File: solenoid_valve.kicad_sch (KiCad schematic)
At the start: 7 parts, among them J17 Conn_01x02_Socket, Q1 Q_NMOS_GSD, U9 TLP785

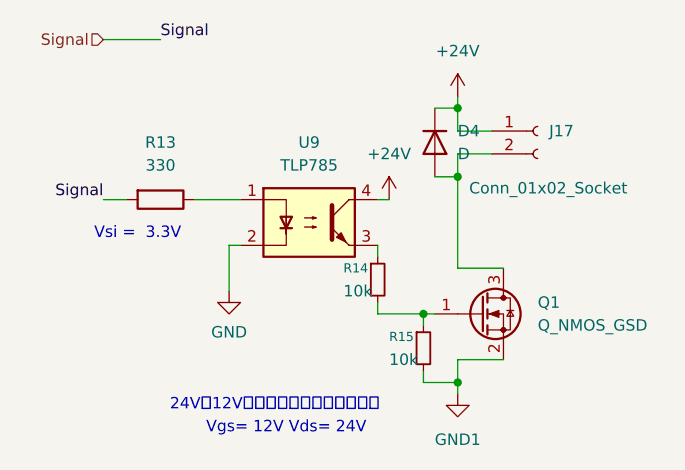
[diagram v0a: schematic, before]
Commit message: サーボときんていをつけ忘れていたので回路図に追加(部品配置に悩んでる
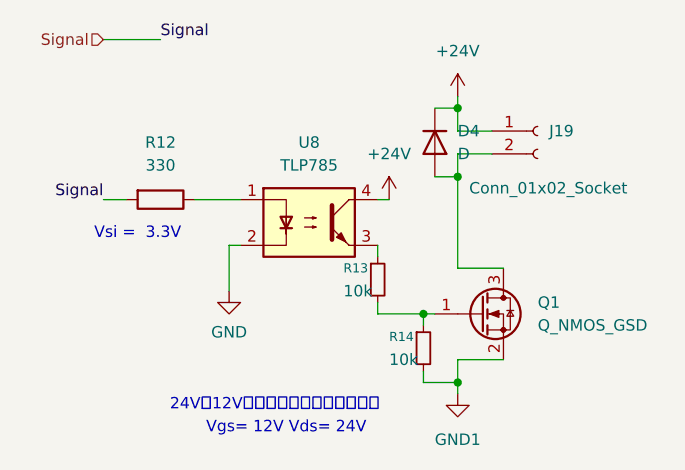
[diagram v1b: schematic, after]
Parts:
- renumbered J17 to J19, R13 to R12, R14 to R13, R15 to R14, U9 to U8
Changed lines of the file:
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@@
 		(in_pos_files yes)
 		(dnp no)
-		(property "Reference" "J17"
+		(property "Reference" "J19"
 			(at 130.81 59.6899 0)
 			(show_name no)
@@
 			(project "ARSTM2602"
 				(path "/537f457d-9719-41ea-89c7-39afb0f25936/1b1d3c2c-89c2-4210-b4e2-6e7b33b504ab"
+					(reference "J22")
+					(unit 1)
+				)
+				(path "/537f457d-9719-41ea-89c7-39afb0f25936/3c4eddd9-2f6c-48df-bbb7-01288ca35755"
+					(reference "J21")
+					(unit 1)
+				)
+				(path "/537f457d-9719-41ea-89c7-39afb0f25936/70727c92-d750-4c7e-95c8-20e0820def0e"
+					(reference "J19")
+					(unit 1)
+				)
+				(path "/537f457d-9719-41ea-89c7-39afb0f25936/884f7e7d-b238-4bb6-a1d8-53bdfde88689"
+					(reference "J23")
+					(unit 1)
+				)
+				(path "/537f457d-9719-41ea-89c7-39afb0f25936/e0dbbca2-494e-4b2c-9270-2b014d7f4a27"
 					(reference "J20")
-					(unit 1)
-				)
-				(path "/537f457d-9719-41ea-89c7-39afb0f25936/3c4eddd9-2f6c-48df-bbb7-01288ca35755"
-					(reference "J19")
-					(unit 1)
-				)
-				(path "/537f457d-9719-41ea-89c7-39afb0f25936/70727c92-d750-4c7e-95c8-20e0820def0e"
-					(reference "J17")
-					(unit 1)
-				)
-				(path "/537f457d-9719-41ea-89c7-39afb0f25936/884f7e7d-b238-4bb6-a1d8-53bdfde88689"
-					(reference "J21")
-					(unit 1)
-				)
-				(path "/537f457d-9719-41ea-89c7-39afb0f25936/e0dbbca2-494e-4b2c-9270-2b014d7f4a27"
-					(reference "J18")
 					(unit 1)
 				)
@@
 		(dnp no)
 		(fields_autoplaced yes)
-		(property "Reference" "#PWR052"
+		(property "Reference" "#PWR057"
 			(at 120.65 59.69 0)
 			(hide yes)
@@
 			(project "ARSTM2602"
 				(path "/537f457d-9719-41ea-89c7-39afb0f25936/1b1d3c2c-89c2-4210-b4e2-6e7b33b504ab"
-					(reference "#PWR064")
+					(reference "#PWR069")
 					(unit 1)
 				)
 				(path "/537f457d-9719-41ea-89c7-39afb0f25936/3c4eddd9-2f6c-48df-bbb7-01288ca35755"
-					(reference "#PWR060")
+					(reference "#PWR065")
 					(unit 1)
 				)
 				(path "/537f457d-9719-41ea-89c7-39afb0f25936/70727c92-d750-4c7e-95c8-20e0820def0e"
-					(reference "#PWR052")
+					(reference "#PWR057")
 					(unit 1)
 				)
 				(path "/537f457d-9719-41ea-89c7-39afb0f25936/884f7e7d-b238-4bb6-a1d8-53bdfde88689"
-					(reference "#PWR068")
+					(reference "#PWR073")
 					(unit 1)
 				)
 				(path "/537f457d-9719-41ea-89c7-39afb0f25936/e0dbbca2-494e-4b2c-9270-2b014d7f4a27"
-					(reference "#PWR056")
+					(reference "#PWR061")
 					(unit 1)
 				)
@@
 		(in_pos_files yes)
 		(dnp no)
-		(property "Reference" "R14"
+		(property "Reference" "R13"
 			(at 107.95 74.93 0)
 			(show_name no)
@@
 			(project "ARSTM2602"
 				(path "/537f457d-9719-41ea-89c7-39afb0f25936/1b1d3c2c-89c2-4210-b4e2-6e7b33b504ab"
-					(reference "R23")
+					(reference "R22")
 					(unit 1)
 				)
 				(path "/537f457d-9719-41ea-89c7-39afb0f25936/3c4eddd9-2f6c-48df-bbb7-01288ca35755"
-					(reference "R20")
+					(reference "R19")
 					(unit 1)
 				)
 				(path "/537f457d-9719-41ea-89c7-39afb0f25936/70727c92-d750-4c7e-95c8-20e0820def0e"
-					(reference "R14")
+					(reference "R13")
 					(unit 1)
 				)
 				(path "/537f457d-9719-41ea-89c7-39afb0f25936/884f7e7d-b238-4bb6-a1d8-53bdfde88689"
-					(reference "R26")
+					(reference "R25")
 					(unit 1)
 				)
 				(path "/537f457d-9719-41ea-89c7-39afb0f25936/e0dbbca2-494e-4b2c-9270-2b014d7f4a27"
-					(reference "R17")
+					(reference "R16")
 					(unit 1)
 				)
@@
 		(dnp no)
 		(fields_autoplaced yes)
-		(property "Reference" "#PWR051"
+		(property "Reference" "#PWR056"
 			(at 113.03 71.12 0)
 			(hide yes)
@@
 			(project "ARSTM2602"
 				(path "/537f457d-9719-41ea-89c7-39afb0f25936/1b1d3c2c-89c2-4210-b4e2-6e7b33b504ab"
-					(reference "#PWR063")
+					(reference "#PWR068")
 					(unit 1)
 				)
 				(path "/537f457d-9719-41ea-89c7-39afb0f25936/3c4eddd9-2f6c-48df-bbb7-01288ca35755"
-					(reference "#PWR059")
+					(reference "#PWR064")
 					(unit 1)
 				)
 				(path "/537f457d-9719-41ea-89c7-39afb0f25936/70727c92-d750-4c7e-95c8-20e0820def0e"
-					(reference "#PWR051")
+					(reference "#PWR056")
 					(unit 1)
 				)
 				(path "/537f457d-9719-41ea-89c7-39afb0f25936/884f7e7d-b238-4bb6-a1d8-53bdfde88689"
-					(reference "#PWR067")
+					(reference "#PWR072")
 					(unit 1)
 				)
 				(path "/537f457d-9719-41ea-89c7-39afb0f25936/e0dbbca2-494e-4b2c-9270-2b014d7f4a27"
-					(reference "#PWR055")
+					(reference "#PWR060")
 					(unit 1)
 				)
@@
 		(in_pos_files yes)
 		(dnp no)
-		(property "Reference" "#PWR050"
+		(property "Reference" "#PWR055"
 			(at 95.25 83.82 0)
 			(hide yes)
@@
 			(project "ARSTM2602"
 				(path "/537f457d-9719-41ea-89c7-39afb0f25936/1b1d3c2c-89c2-4210-b4e2-6e7b33b504ab"
-					(reference "#PWR062")
+					(reference "#PWR067")
 					(unit 1)
 				)
 				(path "/537f457d-9719-41ea-89c7-39afb0f25936/3c4eddd9-2f6c-48df-bbb7-01288ca35755"
-					(reference "#PWR058")
+					(reference "#PWR063")
 					(unit 1)
 				)
 				(path "/537f457d-9719-41ea-89c7-39afb0f25936/70727c92-d750-4c7e-95c8-20e0820def0e"
-					(reference "#PWR050")
+					(reference "#PWR055")
 					(unit 1)
 				)
 				(path "/537f457d-9719-41ea-89c7-39afb0f25936/884f7e7d-b238-4bb6-a1d8-53bdfde88689"
-					(reference "#PWR066")
+					(reference "#PWR071")
 					(unit 1)
 				)
 				(path "/537f457d-9719-41ea-89c7-39afb0f25936/e0dbbca2-494e-4b2c-9270-2b014d7f4a27"
-					(reference "#PWR054")
+					(reference "#PWR059")
 					(unit 1)
 				)
@@
 		(dnp no)
 		(fields_autoplaced yes)
-		(property "Reference" "R13"
+		(property "Reference" "R12"
 			(at 87.63 60.96 90)
 			(show_name no)
@@
 			(project "ARSTM2602"
 				(path "/537f457d-9719-41ea-89c7-39afb0f25936/1b1d3c2c-89c2-4210-b4e2-6e7b33b504ab"
-					(reference "R22")
+					(reference "R21")
 					(unit 1)
 				)
 				(path "/537f457d-9719-41ea-89c7-39afb0f25936/3c4eddd9-2f6c-48df-bbb7-01288ca35755"
-					(reference "R19")
+					(reference "R18")
 					(unit 1)
 				)
 				(path "/537f457d-9719-41ea-89c7-39afb0f25936/70727c92-d750-4c7e-95c8-20e0820def0e"
-					(reference "R13")
+					(reference "R12")
 					(unit 1)
 				)
 				(path "/537f457d-9719-41ea-89c7-39afb0f25936/884f7e7d-b238-4bb6-a1d8-53bdfde88689"
-					(reference "R25")
+					(reference "R24")
 					(unit 1)
 				)
 				(path "/537f457d-9719-41ea-89c7-39afb0f25936/e0dbbca2-494e-4b2c-9270-2b014d7f4a27"
-					(reference "R16")
+					(reference "R15")
 					(unit 1)
 				)
@@
 		(in_pos_files yes)
 		(dnp no)
-		(property "Reference" "R15"
+		(property "Reference" "R14"
 			(at 113.03 82.55 0)
 			(show_name no)
@@
 			(project "ARSTM2602"
 				(path "/537f457d-9719-41ea-89c7-39afb0f25936/1b1d3c2c-89c2-4210-b4e2-6e7b33b504ab"
-					(reference "R24")
+					(reference "R23")
 					(unit 1)
 				)
 				(path "/537f457d-9719-41ea-89c7-39afb0f25936/3c4eddd9-2f6c-48df-bbb7-01288ca35755"
-					(reference "R21")
+					(reference "R20")
 					(unit 1)
 				)
 				(path "/537f457d-9719-41ea-89c7-39afb0f25936/70727c92-d750-4c7e-95c8-20e0820def0e"
-					(reference "R15")
+					(reference "R14")
 					(unit 1)
 				)
 				(path "/537f457d-9719-41ea-89c7-39afb0f25936/884f7e7d-b238-4bb6-a1d8-53bdfde88689"
-					(reference "R27")
+					(reference "R26")
 					(unit 1)
 				)
 				(path "/537f457d-9719-41ea-89c7-39afb0f25936/e0dbbca2-494e-4b2c-9270-2b014d7f4a27"
-					(reference "R18")
+					(reference "R17")
 					(unit 1)
 				)
@@
 		(dnp no)
 		(fields_autoplaced yes)
-		(property "Reference" "#PWR053"
+		(property "Reference" "#PWR058"
 			(at 120.65 95.25 0)
 			(hide yes)
@@
 			(project "ARSTM2602"
 				(path "/537f457d-9719-41ea-89c7-39afb0f25936/1b1d3c2c-89c2-4210-b4e2-6e7b33b504ab"
-					(reference "#PWR065")
+					(reference "#PWR070")
 					(unit 1)
 				)
 				(path "/537f457d-9719-41ea-89c7-39afb0f25936/3c4eddd9-2f6c-48df-bbb7-01288ca35755"
-					(reference "#PWR061")
+					(reference "#PWR066")
 					(unit 1)
 				)
 				(path "/537f457d-9719-41ea-89c7-39afb0f25936/70727c92-d750-4c7e-95c8-20e0820def0e"
-					(reference "#PWR053")
+					(reference "#PWR058")
 					(unit 1)
 				)
 				(path "/537f457d-9719-41ea-89c7-39afb0f25936/884f7e7d-b238-4bb6-a1d8-53bdfde88689"
-					(reference "#PWR069")
+					(reference "#PWR074")
 					(unit 1)
 				)
 				(path "/537f457d-9719-41ea-89c7-39afb0f25936/e0dbbca2-494e-4b2c-9270-2b014d7f4a27"
-					(reference "#PWR057")
+					(reference "#PWR062")
 					(unit 1)
 				)
@@
 		(dnp no)
 		(fields_autoplaced yes)
-		(property "Reference" "U9"
+		(property "Reference" "U8"
 			(at 104.14 60.96 0)
 			(show_name no)
@@
 			(project "ARSTM2602"
 				(path "/537f457d-9719-41ea-89c7-39afb0f25936/1b1d3c2c-89c2-4210-b4e2-6e7b33b504ab"
+					(reference "U11")
+					(unit 1)
+				)
+				(path "/537f457d-9719-41ea-89c7-39afb0f25936/3c4eddd9-2f6c-48df-bbb7-01288ca35755"
+					(reference "U10")
+					(unit 1)
+				)
+				(path "/537f457d-9719-41ea-89c7-39afb0f25936/70727c92-d750-4c7e-95c8-20e0820def0e"
+					(reference "U8")
+					(unit 1)
+				)
+				(path "/537f457d-9719-41ea-89c7-39afb0f25936/884f7e7d-b238-4bb6-a1d8-53bdfde88689"
 					(reference "U12")
 					(unit 1)
 				)
-				(path "/537f457d-9719-41ea-89c7-39afb0f25936/3c4eddd9-2f6c-48df-bbb7-01288ca35755"
-					(reference "U11")
-					(unit 1)
-				)
-				(path "/537f457d-9719-41ea-89c7-39afb0f25936/70727c92-d750-4c7e-95c8-20e0820def0e"
+				(path "/537f457d-9719-41ea-89c7-39afb0f25936/e0dbbca2-494e-4b2c-9270-2b014d7f4a27"
 					(reference "U9")
 					(unit 1)
 				)
-				(path "/537f457d-9719-41ea-89c7-39afb0f25936/884f7e7d-b238-4bb6-a1d8-53bdfde88689"
-					(reference "U13")
-					(unit 1)
-				)
-				(path "/537f457d-9719-41ea-89c7-39afb0f25936/e0dbbca2-494e-4b2c-9270-2b014d7f4a27"
-					(reference "U10")
-					(unit 1)
-				)
